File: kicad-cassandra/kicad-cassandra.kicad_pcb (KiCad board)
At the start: 4 copper layers, 48 x 106.5 mm, 63 parts, among them J1 Conn_ST_STDC14, J2 USB_C_Receptacle_USB2.0_16P, J3 DE9_Pins_MountingHoles, J4 Conn_ST_STDC14, J5 Conn_02x10_Odd_Even, J6 Micro_SD_Card_Det1, SW1 SW_Push, SW2 SW_Push, SW3 SW_Push, SW4 SW_SPDT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

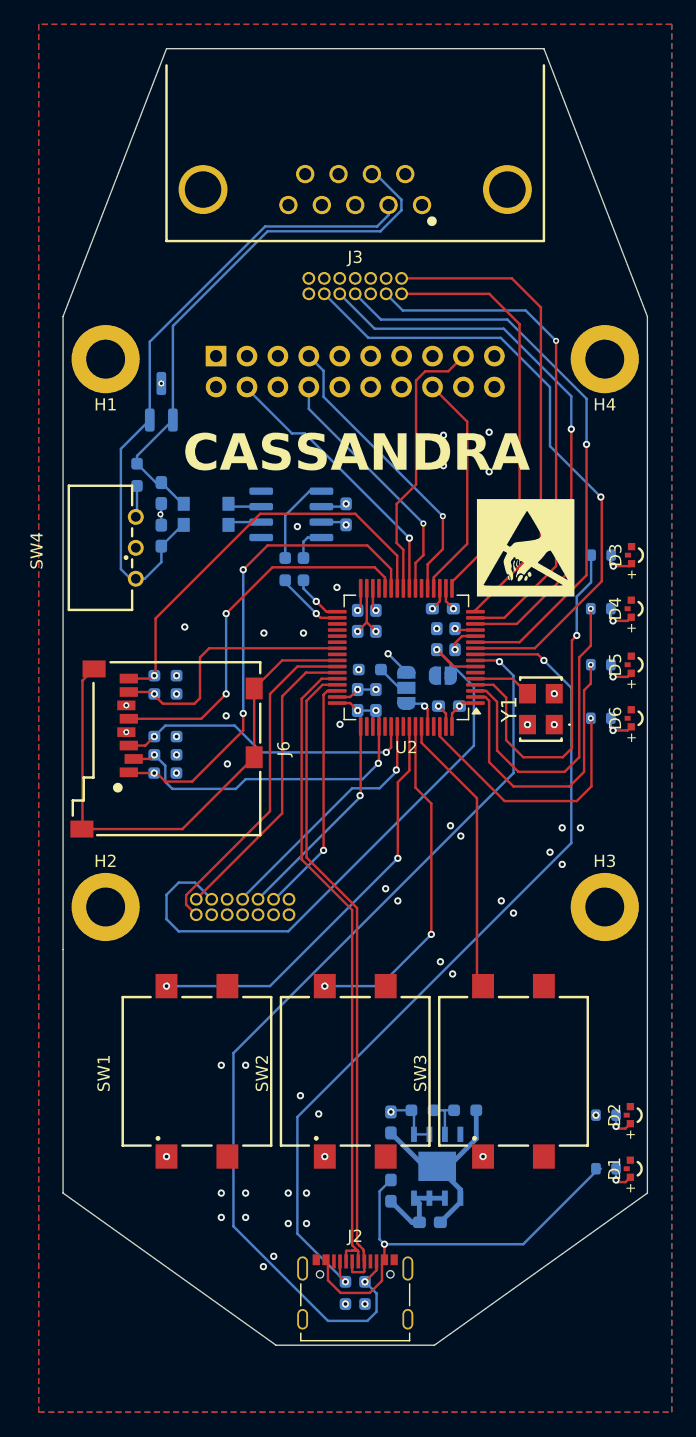
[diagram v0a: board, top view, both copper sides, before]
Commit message: use rohm ldo
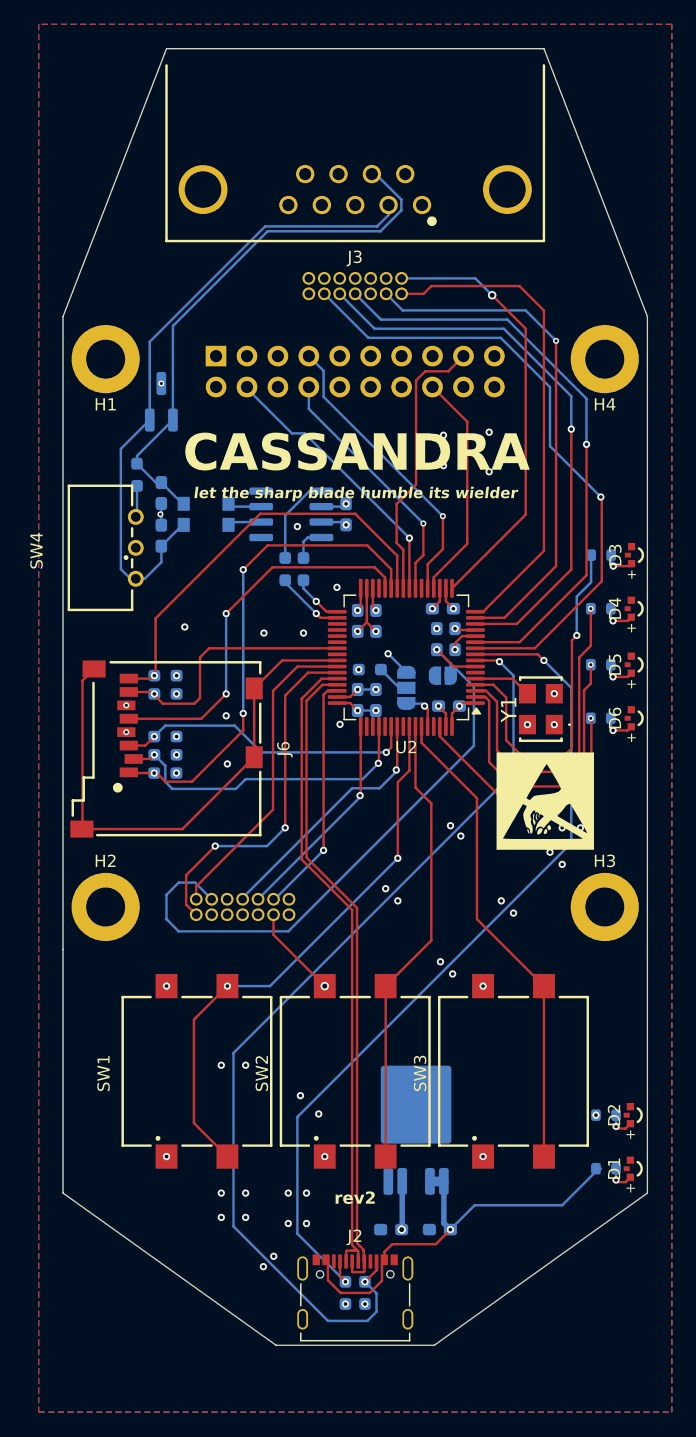
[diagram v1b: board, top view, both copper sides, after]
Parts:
- removed F1: 1500m, Fuse:Fuse_0603_1608Metric_Pad1.05x0.95mm_HandSolder
- removed R2: 1.27k, Resistor_SMD:R_0603_1608Metric_Pad0.98x0.95mm_HandSolder
- removed R3: 220, Resistor_SMD:R_0603_1608Metric_Pad0.98x0.95mm_HandSolder
- U1: value MIC69153YME-TR -> BD33FC0WFP; footprint cassandra:SOIC-8_ME_MCH-L -> Package_TO_SOT_SMD:TO-252-4
- moved G*** 20.9 mm to (89.6, 89.8)
- moved C4 8.80 mm to (77.0, 125.0), turned to 180 degrees
- moved U1 4.18 mm to (79.0, 116.0)
- moved C3 1.02 mm to (81.0, 125.0), turned to 180 degrees
- turned JP2 to 90 degrees
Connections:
- C3 pad 1: Net-(U1-EN) -> VDD
- U1 pad 1: GND -> VDD
- U1 pad 2: Net-(U1-EN) -> VDD
- U1 pad 3: Net-(U1-EN) -> GND
- U1 pad 5: Net-(U1-SNS/ADJ) -> unconnected-(U1-NC-Pad5)
- U2 pad 16: /TGT_VCP_RX -> /TGT_VCP_TX
- U2 pad 17: /TGT_VCP_TX -> /TGT_VCP_RX
- U2 pad 42: /HOST_VCP_RX -> /HOST_VCP_TX
- U2 pad 43: /HOST_VCP_TX -> /HOST_VCP_RX
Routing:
- net GND: track 36.1 -> 18.6 mm
- net /PBT_2: track 23.4 -> 39.5 mm
- net /PBT_0: track 34.6 -> 45.8 mm
- net /PBT_1: track 28.1 -> 37.4 mm, vias 2 -> 0
- net Net-(U1-EN): track 7.75 -> 0.00 mm
- net +3.3V: track 22.9 -> 28.9 mm, vias 21 -> 24
- net /TGT_VCP_TX: track 34.7 -> 40.2 mm
- net /TGT_VCP_RX: track 39.7 -> 35.7 mm, vias 0 -> 1
- net Net-(U1-SNS/ADJ): track 3.67 -> 0.00 mm
- net /HOST_VCP_RX: track 27.8 -> 29.3 mm, vias 0 -> 2
- net Net-(JP2-A): track 2.12 -> 3.36 mm
- net /HOST_VCP_TX: track 24.9 -> 25.8 mm
- net VDD: track 36.1 -> 35.3 mm
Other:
- board text added: "rev2"

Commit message: add wire only possibility
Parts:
- removed D3, D4, D5, D6: AMBER, cassandra:WL-SMSW_0603_ROUND
- removed R4, R5, R6, R7: 230, Resistor_SMD:R_0603_1608Metric
- added J7: ~, cassandra:CONN4_05010302_WRE, B.Cu at (86.5, 69.5)
- added J8: ~, cassandra:CONN4_05010302_WRE, B.Cu at (62.0, 113.9)
- D1, D2: footprint cassandra:WL-SMSW_0603_ROUND -> LED_SMD:LED_0603_1608Metric_Pad1.05x0.95mm_HandSolder
- moved D1 0.85 mm to (95.8, 120.0)
- moved D2 0.85 mm to (95.8, 115.6)
- moved R8 0.85 mm to (93.8, 120.0)
- moved R9 0.85 mm to (93.8, 115.6)
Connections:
- J2 pad A5: /USB_CC1_READ -> Net-(J2-CC1)
- J2 pad B5: /USB_CC2_READ -> Net-(J2-CC2)
- R10 pad 1: /USB_CC1_READ -> Net-(J2-CC1)
- R11 pad 1: /USB_CC2_READ -> Net-(J2-CC2)
- U2 pad 2: /LED_BIT2 -> unconnected-(U2-PC13-Pad2)
- U2 pad 3: /LED_BIT1 -> unconnected-(U2-PC14-Pad3)
- U2 pad 4: /LED_BIT0 -> unconnected-(U2-PC15-Pad4)
- U2 pad 62: /LED_BIT3 -> unconnected-(U2-PB9-Pad62)
- U2 pad 8: /USB_CC2_READ -> unconnected-(U2-PC0-Pad8)
- U2 pad 9: /USB_CC1_READ -> unconnected-(U2-PC1-Pad9)
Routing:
- net /USB_CC2_READ: track 78.6 -> 0.00 mm, vias 2 -> 0
- net /USB_CC1_READ: track 70.6 -> 0.00 mm, vias 2 -> 0
- net /CAN/CAN_LOW: track 52.5 -> 93.5 mm
- net /CAN/CAN_HIGH: track 44.6 -> 84.6 mm
- net VDD: track 35.3 -> 68.5 mm
- net /LED_BIT0: track 29.6 -> 0.00 mm, vias 1 -> 0
- net /LED_BIT1: track 26.7 -> 0.00 mm, vias 1 -> 0
- net /LED_BIT2: track 24.4 -> 0.00 mm, vias 1 -> 0
- net /LED_BIT3: track 21.6 -> 0.00 mm, vias 1 -> 0
- net GND: track 18.6 -> 32.5 mm, vias 54 -> 24
- net /DISPLAY_SPI_SDIN: track 20.8 -> 25.1 mm
- net /DISPLAY_DC: track 22.7 -> 26.9 mm
- net /DISPLAY_SPI_SCLK: track 24.2 -> 27.9 mm
- net Net-(D6-A): track 2.70 -> 0.00 mm, vias 1 -> 0
- net Net-(D5-A): track 2.70 -> 0.00 mm, vias 1 -> 0
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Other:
- board text added: "+"
- board text added: "-"
- board text added: "CANH"
- board text added: "CANL"
